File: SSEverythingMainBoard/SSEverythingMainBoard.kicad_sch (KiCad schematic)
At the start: 64 parts, among them J1 CONN_06SILK_FEMALE_PTH, J2 CONN_06SILK_FEMALE_PTH, J3 POWER, J4 Switch, J5 Conn_01x02, J6 Conn_01x05, M1 Left MOTOR, M2 Right MOTOR, SW1 TACT_SW, U1 DFRobot_DC_Controller

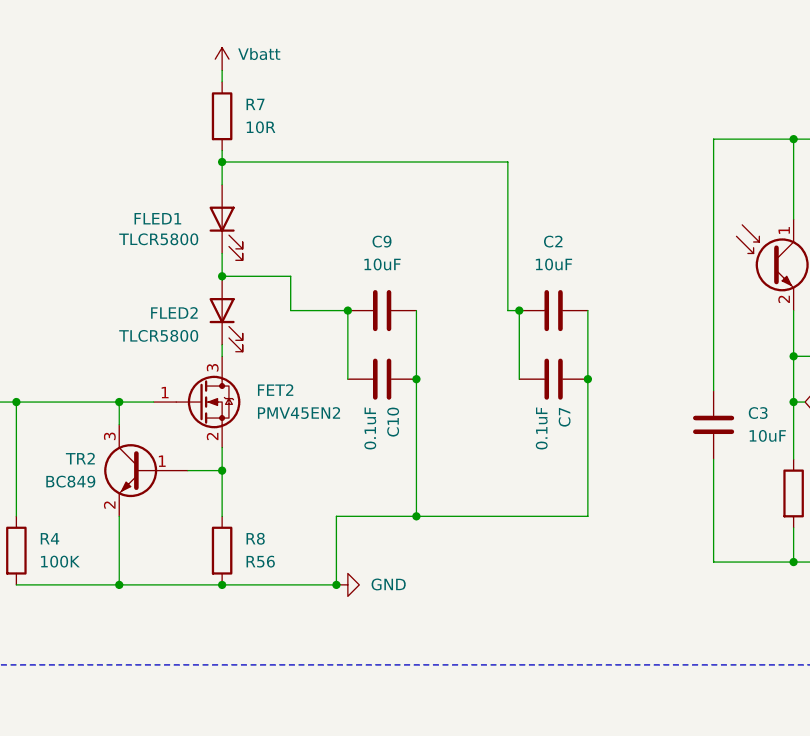
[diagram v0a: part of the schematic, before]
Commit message: before updating to KiCad 9 and changing sensor design
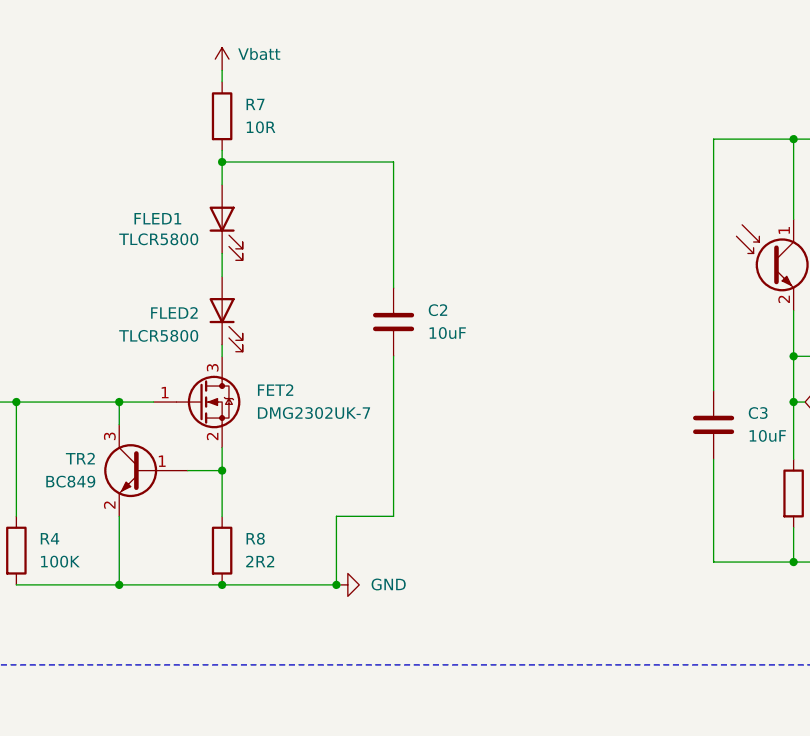
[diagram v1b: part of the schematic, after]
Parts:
- removed C10, C7: 0.1uF, Capacitor_SMD:C_0805_2012Metric_Pad1.18x1.45mm_HandSolder, symbol Device:C
- removed C9: 10uF, Capacitor_SMD:C_0805_2012Metric_Pad1.18x1.45mm_HandSolder, symbol Device:C
- FET2: value PMV45EN2 -> DMG2302UK-7
- R8: value R56 -> 2R2
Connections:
- net GND: now also C2.1; no longer C2.2
- net at FLED1.2 (A), R7.2: now also C2.2; no longer C2.1
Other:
- moved on the sheet: C2
